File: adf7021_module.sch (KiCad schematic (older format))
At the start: 75 parts, among them J1 Conn_Board2Board, J2 Conn_Coaxial, J3 Conn_Coaxial, J4 Conn_goldpin, J5 Conn_Coaxial, J6 Conn_Coaxial, J7 RFShield_OnePiece, U1 ADF7021, X1 19.68MHz

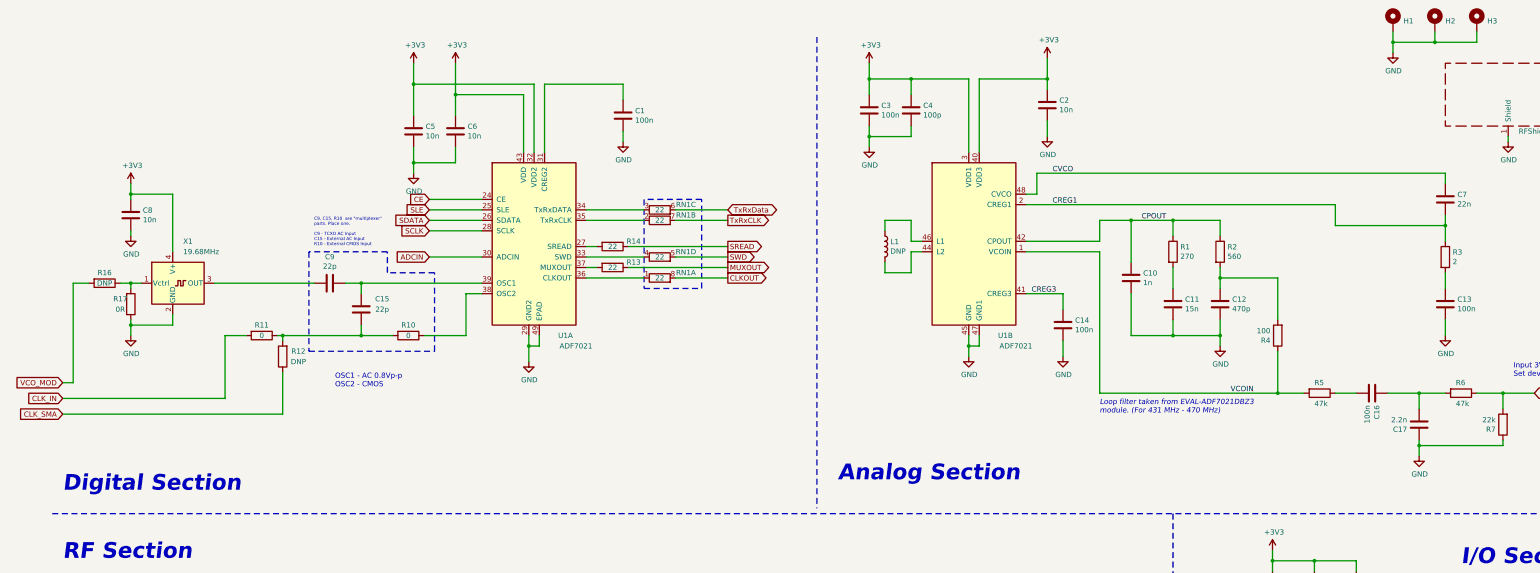
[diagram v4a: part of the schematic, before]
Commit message: adding fab outputs
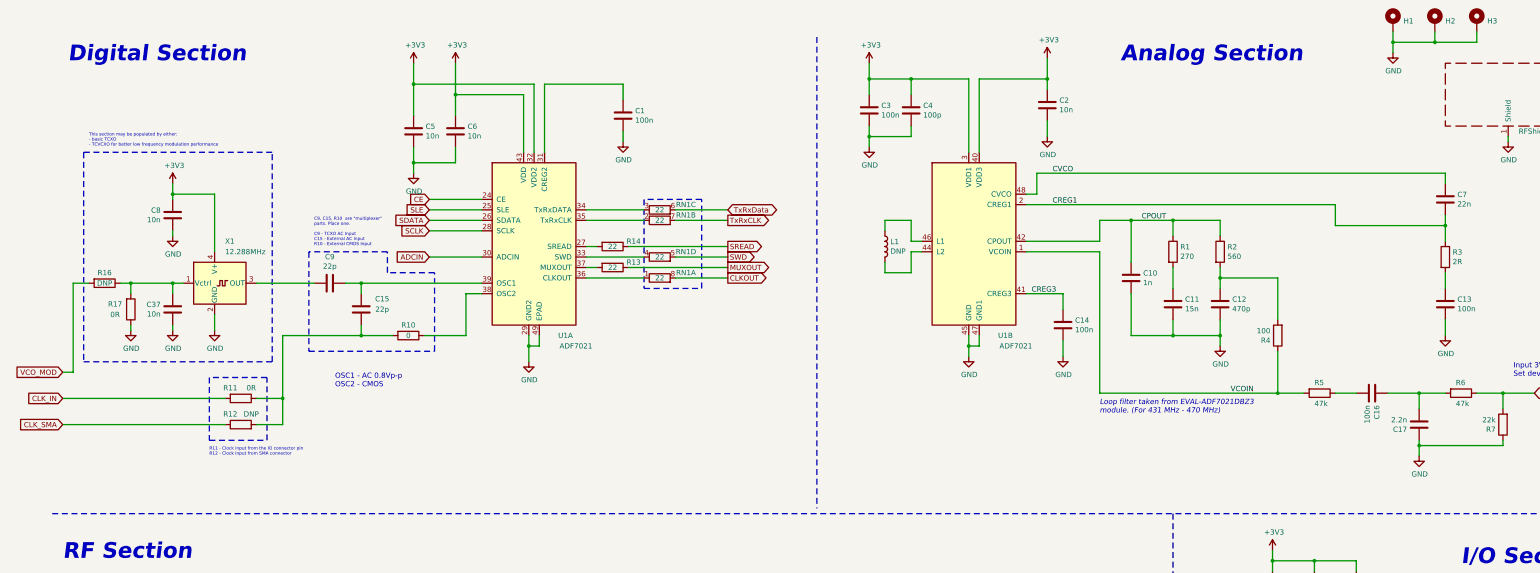
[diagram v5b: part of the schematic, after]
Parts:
- added C37: 10n, Capacitor_SMD:C_0402_1005Metric_Pad0.74x0.62mm_HandSolder, symbol Device:C
- R11: value 0 -> 0R
- R3: value 2 -> 2R
- X1: value 19.68MHz -> 12.288MHz
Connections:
- net GND: now also C37.2
- net at R16.1, R17.2, X1.1 (Vctrl): now also C37.1
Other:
- note added: "R11 - Clock input from the IO connector pin\nR12 - Clock input from SMA connector"
- note added: "This section may be populated by either:\n- basic TCXO\n- TCVCXO for better low frequency modulation performance"
- moved on the sheet: C8, R11, R12, R17, X1
